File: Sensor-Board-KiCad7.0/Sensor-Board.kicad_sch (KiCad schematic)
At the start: 79 parts, among them J1 9401-0-15-15-23-27-10-0, J19 110990030, J2 9401-0-15-15-23-27-10-0, J3 9401-0-15-15-23-27-10-0, J4 9401-0-15-15-23-27-10-0, J5 9401-0-15-15-23-27-10-0, J6 9401-0-15-15-23-27-10-0, J7 9401-0-15-15-23-27-10-0, J8 9401-0-15-15-23-27-10-0, J9 9401-0-15-15-23-27-10-0, U1 OPA396DCKT, U10 BME680, U13 TCA9548AMRGER, U14 OPA396DCKT, U19 MMBFJ177LT1, U2 OPA396DCKT, U20 MMBFJ177LT1, U21 OPA396DCKT, U22 OPA396DCKT, U25 NAU7802SGI, U26 MMBFJ177LT1, U3 OPA396DCKT, U4 NAU7802SGI

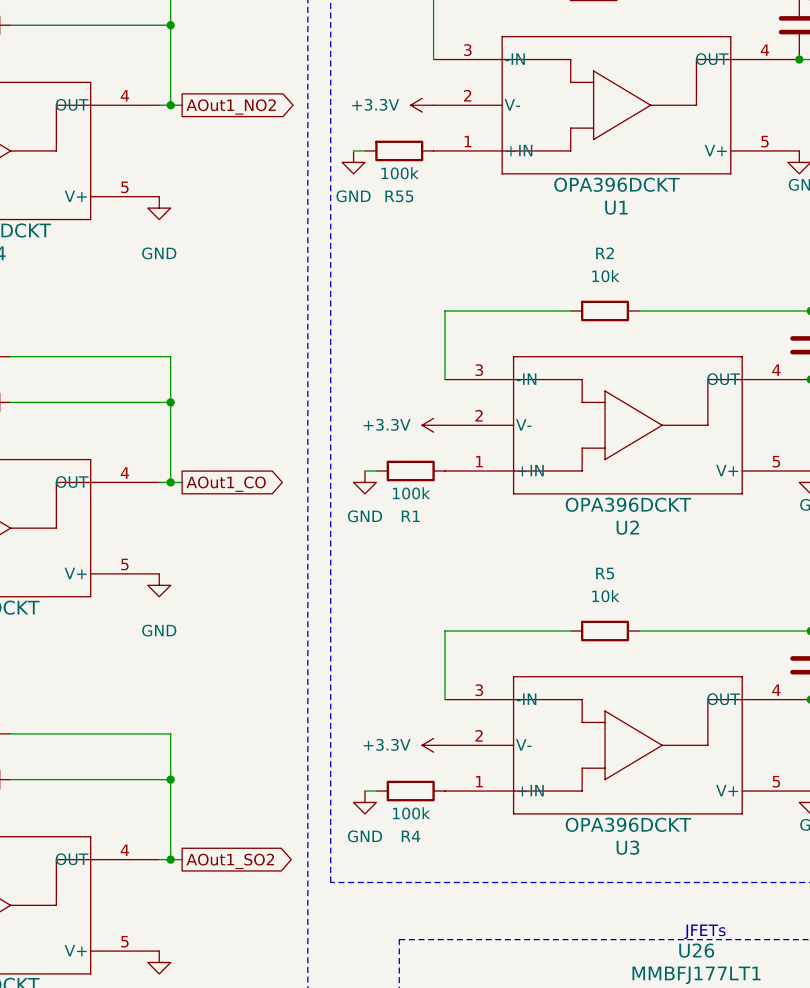
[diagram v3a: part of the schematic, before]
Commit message: Final check of schematic
Double-checked schematic for compliance to datasheets and design requirements. Assigned footprints to all resistors and capacitors
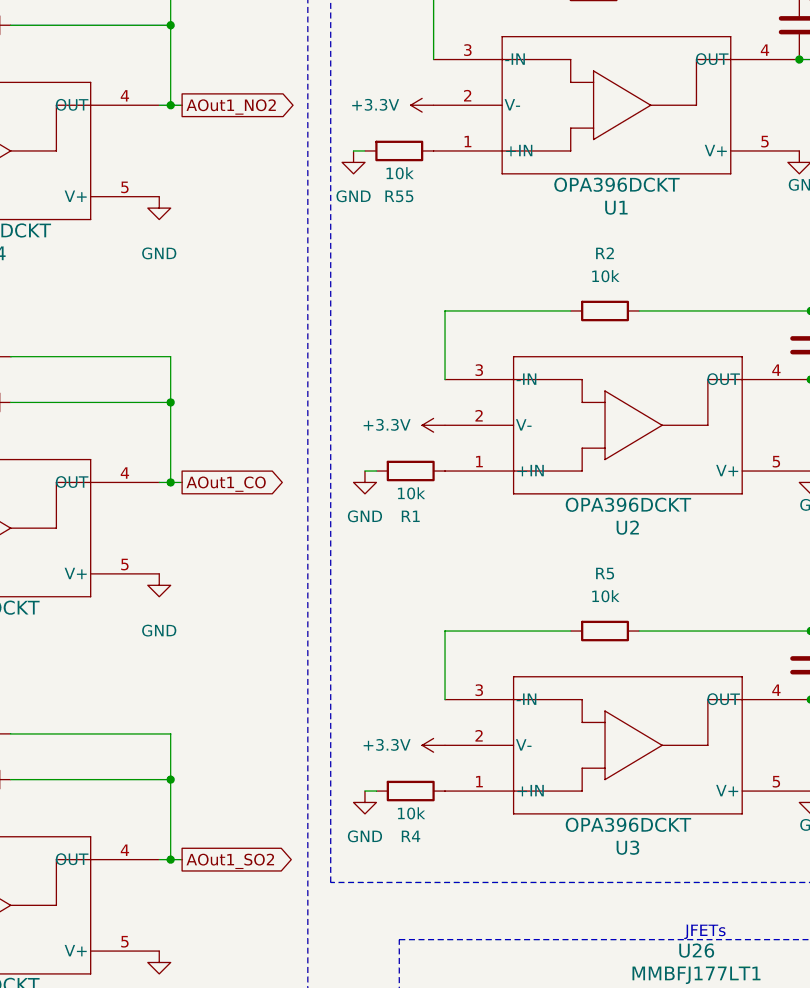
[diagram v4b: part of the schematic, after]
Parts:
- C1, C19, C2, C20, C21, C3, C4, C8, C9: footprint (none) -> Capacitor_SMD:C_0603_1608Metric
- J1, J2, J3, J4, J5, J6, J7, J8, J9: footprint CONN_0384-0-67-80-23-27-10-0_MIM -> EChem socket:CONN_0384-0-67-80-23-27-10-0_MIM
- J19: footprint CONN_110990030_SEE -> I2C Connector:CONN_110990030_SEE
- R1, R4, R55: value 100k -> 10k; footprint (none) -> Resistor_SMD:R_0603_1608Metric
- R19, R2, R20, R21, R22, R23, R24, R25, R26, R27, R28, R29, R3, R30, R31, R32, R33, R34, R41, R42, R46, R5, R52, R53, R54, R56, R57, R6, R67, R68, R69, R7, R8, R9: footprint (none) -> Resistor_SMD:R_0603_1608Metric
- TP1, TP11, TP12, TP13, TP14, TP15, TP16, TP17, TP18, TP2: footprint (none) -> TestPoint:TestPoint_Pad_D1.5mm
- U1, U14, U2, U21, U22, U3: footprint SC_96DCKT_TEX -> OPA396DCKT:SC_96DCKT_TEX
- U19, U20, U26: footprint SOT-23-3_1P4X3P040_ONS -> MMBFJ177LT1G:SOT-23-3_1P4X3P040_ONS
- U25, U4: footprint SOI16_NAU7802SGI_NUV -> NAU7802:SOI16_NAU7802SGI_NUV

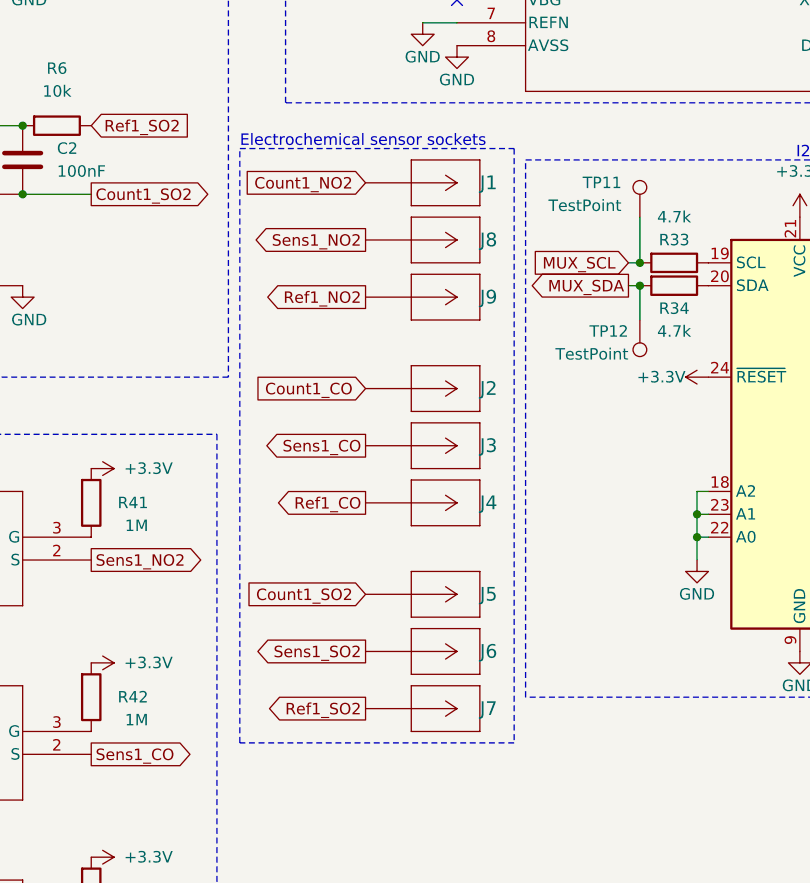
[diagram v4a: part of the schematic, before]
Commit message: Made pin changes to EChem sensors
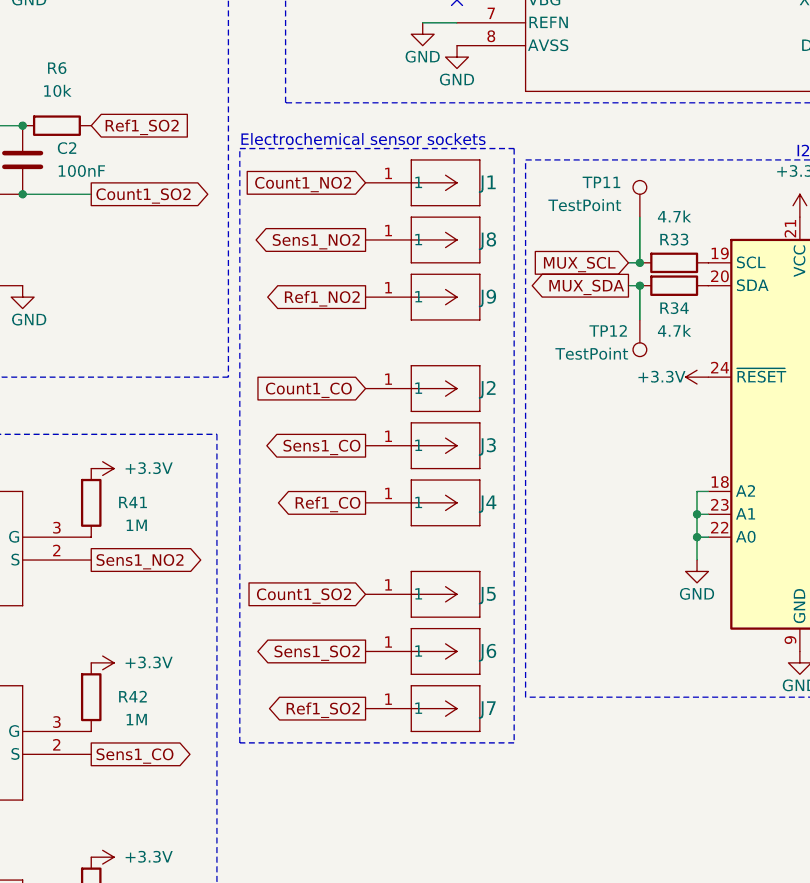
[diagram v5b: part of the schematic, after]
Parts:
- J1, J2, J3, J4, J5, J6, J7, J8, J9: footprint EChem socket:CONN_0384-0-67-80-23-27-10-0_MIM -> CONN_0384-0-67-80-23-27-10-0_MIM
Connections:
- net Count1_CO: now also J2.1; no longer J2.
- net Count1_NO2: now also J1.1; no longer J1.
- net Count1_SO2: now also J5.1; no longer J5.
- net Ref1_CO: now also J4.1; no longer J4.
- net Ref1_NO2: now also J9.1; no longer J9.
- net Ref1_SO2: now also J7.1; no longer J7.
- net Sens1_CO: now also J3.1; no longer J3.
- net Sens1_NO2: now also J8.1; no longer J8.
- net Sens1_SO2: now also J6.1; no longer J6.

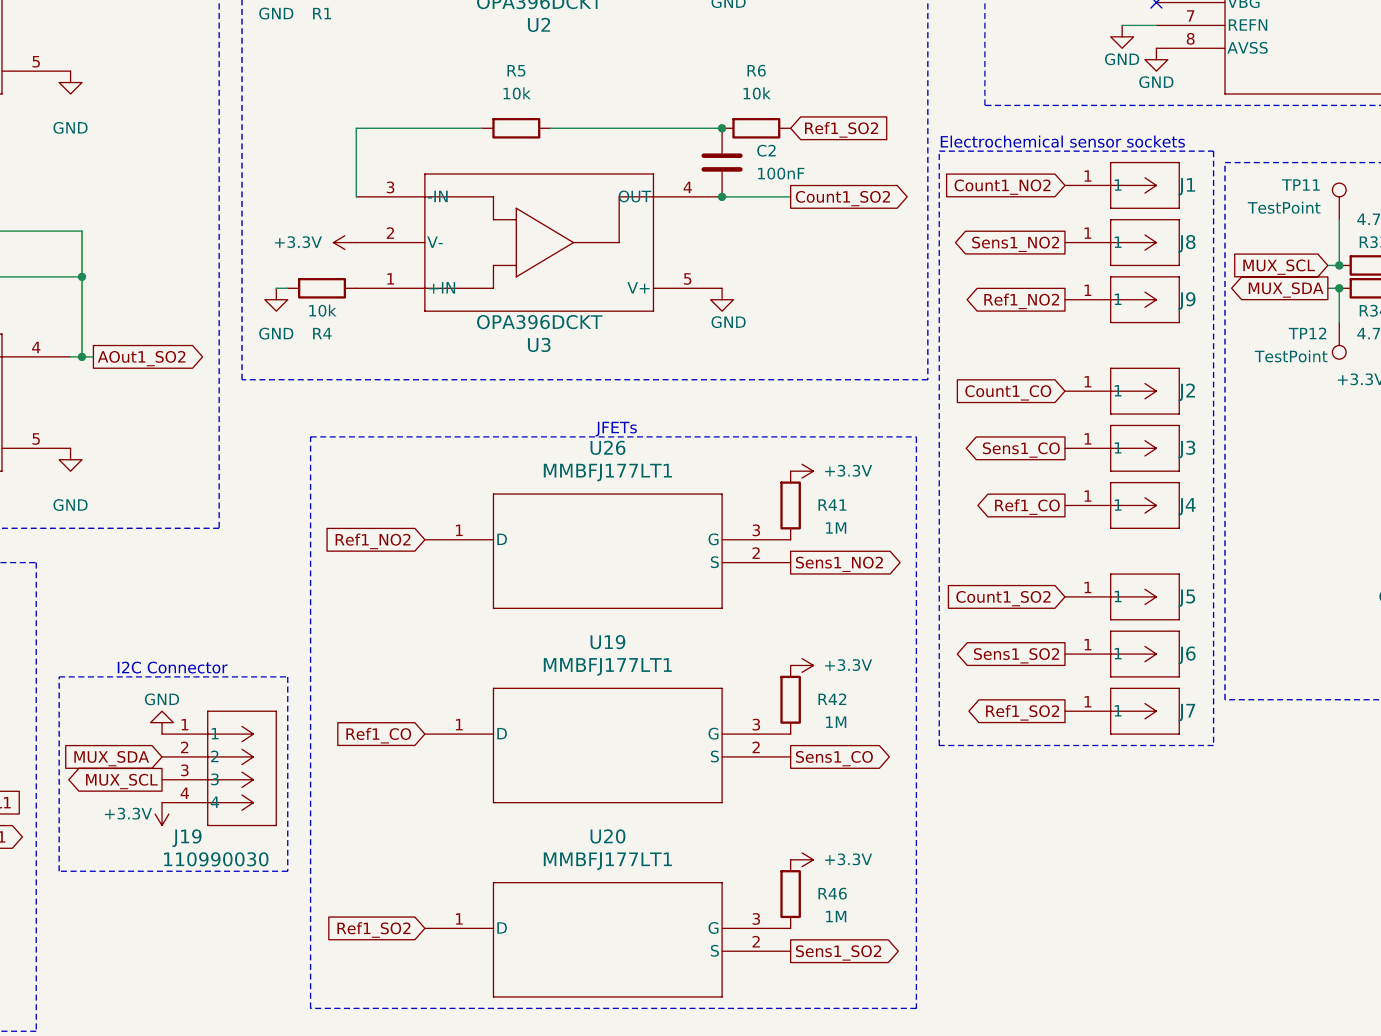
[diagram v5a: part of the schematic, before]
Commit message: Added footprints for components
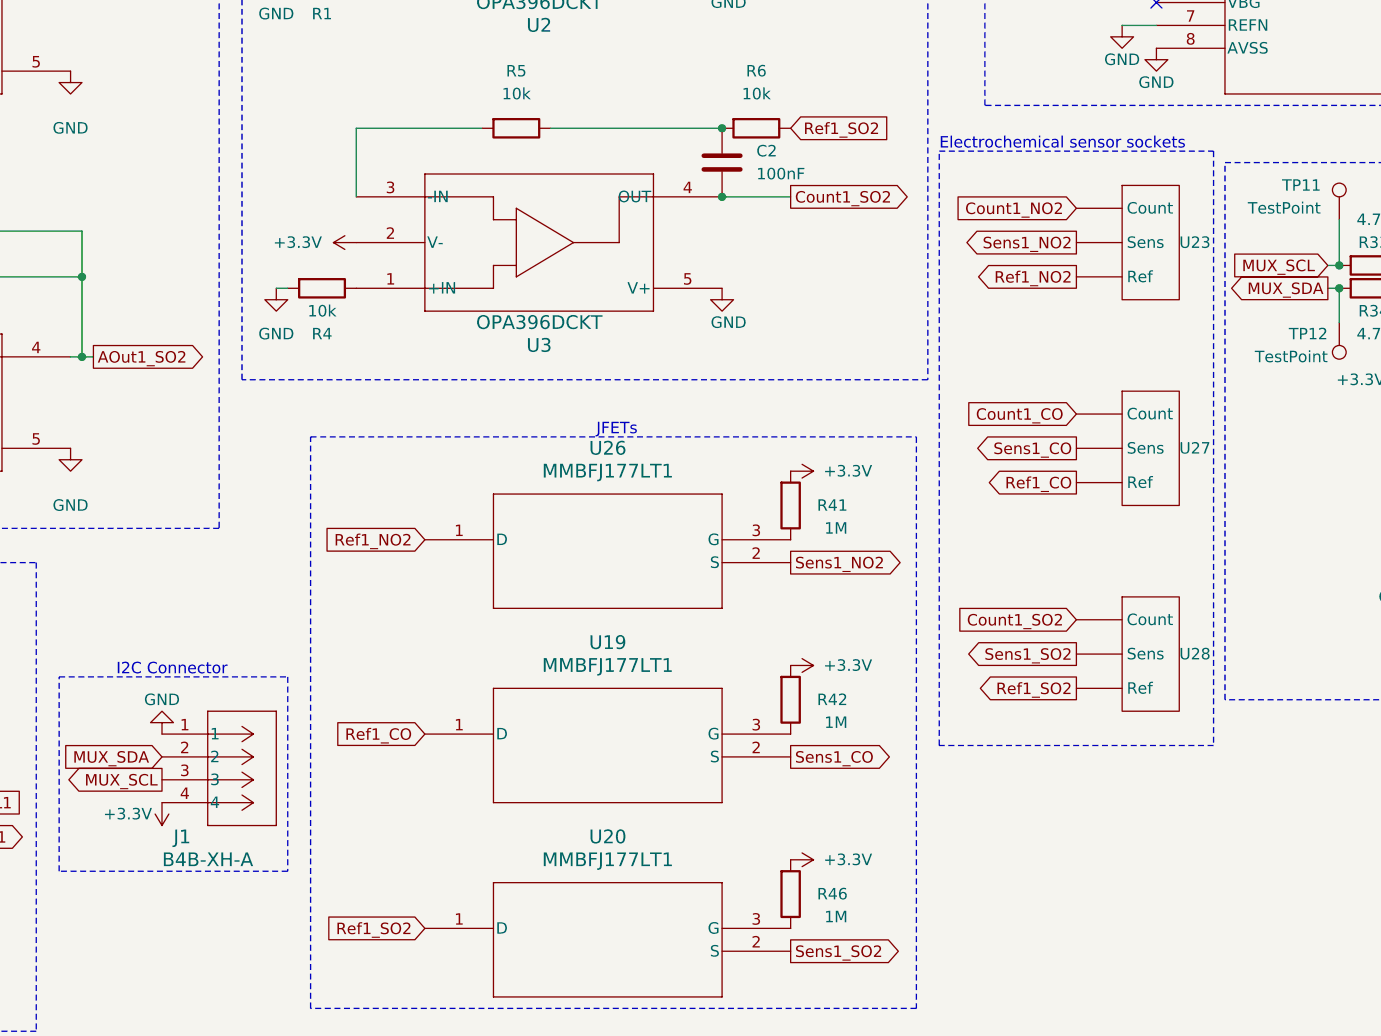
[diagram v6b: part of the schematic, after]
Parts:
- removed J1, J2, J3, J4, J5, J6, J7, J8, J9: 9401-0-15-15-23-27-10-0, CONN_0384-0-67-80-23-27-10-0_MIM, symbol EChem socket:9401-0-15-15-23-27-10-0
- removed J19: 110990030, I2C Connector:CONN_110990030_SEE, symbol I2C Connector:110990030
- added J1: B4B-XH-A, I2C Connector:CONN_B4B-XH-A_JST, symbol I2C Connector:B4B-XH-A
- added U23, U27, U28: ~, EChem socket:3-pin socket, symbol EChem socket:3-pin_socket
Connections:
- net +3.3V: now also J1.4
- net Count1_CO: now also U27. (Sens)
- net Count1_NO2: now also U23. (Sens)
- net Count1_SO2: now also U28. (Sens)
- net GND: now also J1.1
- net MUX_SCL: now also J1.3
- net MUX_SDA: now also J1.2
- net Ref1_CO: now also U27. (Sens)
- net Ref1_NO2: now also U23. (Sens)
- net Ref1_SO2: now also U28. (Sens)
- net Sens1_CO: now also U27. (Sens)
- net Sens1_NO2: now also U23. (Sens)
- net Sens1_SO2: now also U28. (Sens)
